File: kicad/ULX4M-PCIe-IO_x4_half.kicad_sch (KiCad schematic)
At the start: 51 parts, among them J10 FCR684205R, J11 OLED, J12 641737-1, J13 39-30-0060, J14 LM7805_EN, J15 POE, J3 SFP+, J4 SFP+, J5 HAT, J6 EXT_USB, J7 Micro_SD_Card_CD, J8 Board_To_Board, J9 FCR684205T, P1 HDMI-D, SW1 SW_DIP_x08, SW2 SW_DIP_x08, U10 TPD4E02B04DQA, U11 TPD4E02B04DQA, U12 TPD4E02B04DQA, U13 AT24CS32-SSHM, U14 LM78M05_TO252, U9 TPD4E02B04DQA

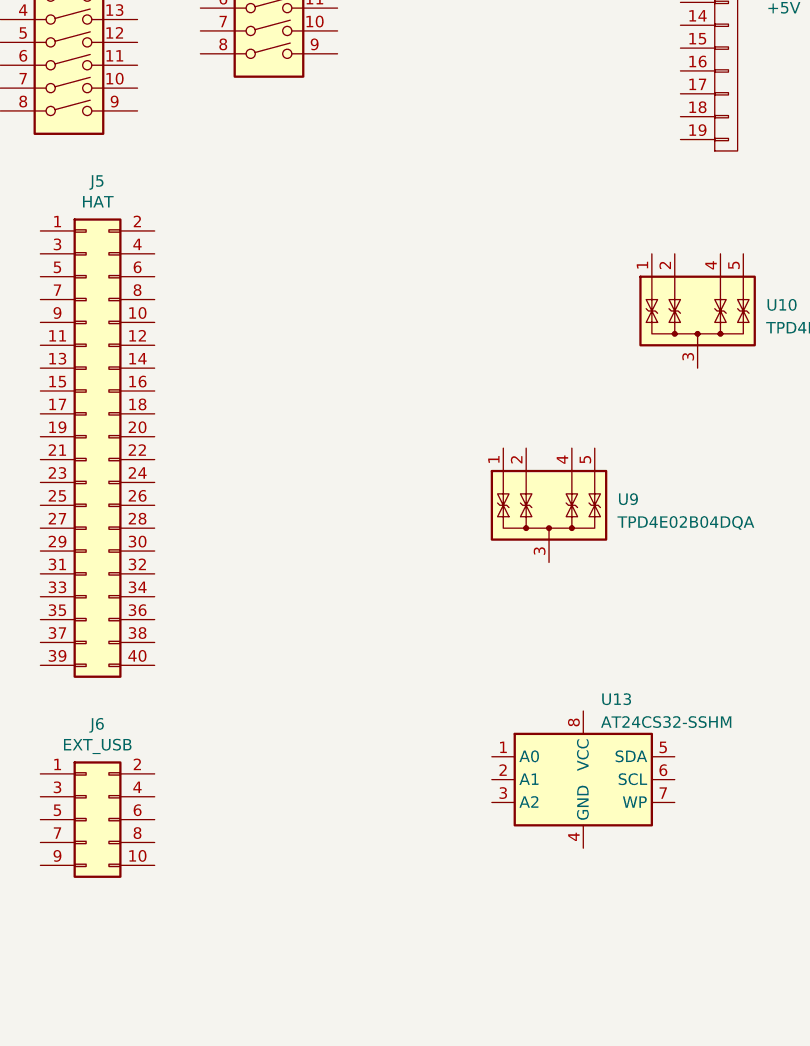
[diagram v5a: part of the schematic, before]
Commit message: Adding barrel connector, adding JTAG, adding new pic
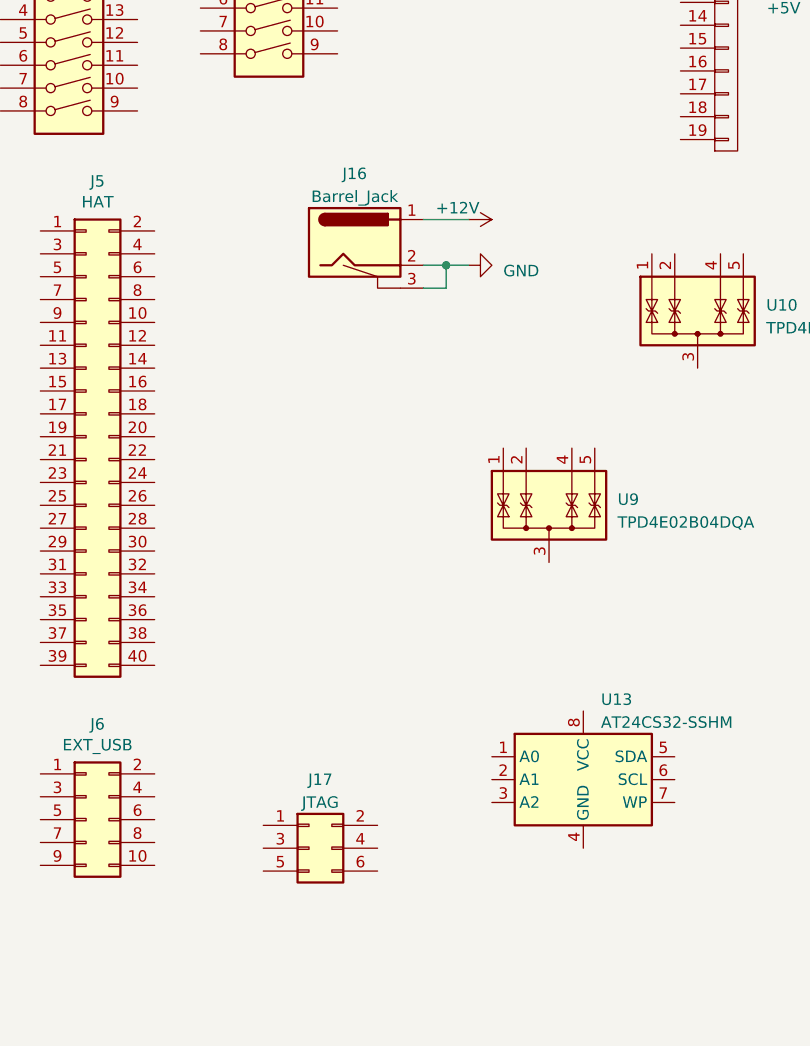
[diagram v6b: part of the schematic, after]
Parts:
- added J16: Barrel_Jack, CM4IO:BarrelJack_Horizontal, symbol CM4IO:Barrel_Jack
- added J17: JTAG, Connector_PinHeader_2.54mm:PinHeader_2x03_P2.54mm_Vertical, symbol Connector_Generic:Conn_02x03_Odd_Even
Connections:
- net +12V: now also J16.1
- net GND: now also J16.2, J16.3
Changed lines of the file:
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@@
   (junction (at 139.7 185.42) (diameter 0) (color 0 0 0 0)
   )
+  (junction (at 200.66 87.63) (diameter 0) (color 0 0 0 0)
+  )
   (junction (at 355.6 54.61) (diameter 0) (color 0 0 0 0)
   )
@@
     (stroke (width 0) (type default))
   )
+  (wire (pts (xy 198.12 87.63) (xy 200.66 87.63))
+    (stroke (width 0) (type default))
+  )
   (wire (pts (xy 355.6 54.61) (xy 365.76 54.61))
     (stroke (width 0) (type default))
   )
+  (wire (pts (xy 200.66 87.63) (xy 203.2 87.63))
+    (stroke (width 0) (type default))
+  )
   (wire (pts (xy 31.75 43.18) (xy 34.29 43.18))
     (stroke (width 0) (type default))
@@
     (stroke (width 0) (type default))
   )
+  (wire (pts (xy 200.66 90.17) (xy 200.66 87.63))
+    (stroke (width 0) (type default))
+  )
   (wire (pts (xy 167.64 187.96) (xy 165.1 187.96))
     (stroke (width 0) (type default))
@@
     (stroke (width 0) (type default))
   )
+  (wire (pts (xy 198.12 82.55) (xy 203.2 82.55))
+    (stroke (width 0) (type default))
+  )
   (wire (pts (xy 57.15 64.77) (xy 59.69 64.77))
+    (stroke (width 0) (type default))
+  )
+  (wire (pts (xy 198.12 90.17) (xy 200.66 90.17))
     (stroke (width 0) (type default))
   )
@@
     )
   )
+  (symbol (lib_id "Connector_Generic:Conn_02x03_Odd_Even") (at 185.42 152.4 0) (unit 1)
+    (in_bom yes) (on_board yes) (dnp no) (fields_autoplaced)
+    (property "Reference" "J17" (at 186.69 144.78 0)
+      (effects (font (size 1.27 1.27)))
+    )
+    (property "Value" "JTAG" (at 186.69 147.32 0)
+      (effects (font (size 1.27 1.27)))
+    )
+    (property "Footprint" "Connector_PinHeader_2.54mm:PinHeader_2x03_P2.54mm_Vertical" (at 185.42 152.4 0)
+      (effects (font (size 1.27 1.27)) hide)
+    )
+    (property "Datasheet" "~" (at 185.42 152.4 0)
+      (effects (font (size 1.27 1.27)) hide)
+    )
+    (pin "1")
+    (pin "2")
+    (pin "3")
+    (pin "4")
+    (pin "5")
+    (pin "6")
+    (instances
+      (project "ULX4M-PCIe-IO_x4_half"
+        (path "/e227bafe-08dc-4b2a-9df8-340d24e6faf1"
+          (reference "J17") (unit 1) (value "JTAG") (footprint "Connector_PinHeader_2.54mm:PinHeader_2x03_P2.54mm_Vertical")
+        )
+      )
+    )
+  )
   (symbol (lib_id "Mechanical:MountingHole") (at 80.01 193.04 0) (unit 1)
     (in_bom yes) (on_board yes) (dnp no) (fields_autoplaced)
@@
     )
   )
+  (symbol (lib_id "power:+12V") (at 203.2 82.55 270) (unit 1)
+    (in_bom yes) (on_board yes) (dnp no)
+    (property "Reference" "#PWR0107" (at 199.39 82.55 0)
+      (effects (font (size 1.27 1.27)) hide)
+    )
+    (property "Value" "+12V" (at 201.93 81.28 90)
+      (effects (font (size 1.27 1.27)))
+    )
+    (property "Footprint" "" (at 203.2 82.55 0)
+      (effects (font (size 1.27 1.27)) hide)
+    )
+    (property "Datasheet" "" (at 203.2 82.55 0)
+      (effects (font (size 1.27 1.27)) hide)
+    )
+    (pin "1")
+    (instances
+      (project "ULX4M-PCIe-IO_x4_half"
+        (path "/e227bafe-08dc-4b2a-9df8-340d24e6faf1/00000000-0000-0000-0000-00005d508b15"
+          (reference "#PWR0107") (unit 1) (value "+12V") (footprint "")
+        )
+        (path "/e227bafe-08dc-4b2a-9df8-340d24e6faf1"
+          (reference "#PWR0137") (unit 1) (value "+12V") (footprint "")
+        )
+      )
+    )
+  )
   (symbol (lib_id "Mechanical:MountingHole") (at 111.76 187.96 0) (unit 1)
     (in_bom yes) (on_board yes) (dnp no) (fields_autoplaced)
@@
         (path "/e227bafe-08dc-4b2a-9df8-340d24e6faf1"
           (reference "C11") (unit 1) (value "10nF") (footprint "Capacitor_SMD:C_0603_1608Metric")
+        )
+      )
+    )
+  )
+  (symbol (lib_id "power:GND") (at 203.2 87.63 90) (unit 1)
+    (in_bom yes) (on_board yes) (dnp no) (fields_autoplaced)
+    (property "Reference" "#PWR0138" (at 209.55 87.63 0)
+      (effects (font (size 1.27 1.27)) hide)
+    )
+    (property "Value" "GND" (at 207.01 88.265 90)
+      (effects (font (size 1.27 1.27)) (justify right))
+    )
+    (property "Footprint" "" (at 203.2 87.63 0)
+      (effects (font (size 1.27 1.27)) hide)
+    )
+    (property "Datasheet" "" (at 203.2 87.63 0)
+      (effects (font (size 1.27 1.27)) hide)
+    )
+    (pin "1")
+    (instances
+      (project "ULX4M-PCIe-IO_x4_half"
+        (path "/e227bafe-08dc-4b2a-9df8-340d24e6faf1"
+          (reference "#PWR0138") (unit 1) (value "GND") (footprint "")
         )
       )
@@
         )
       )
+    )
+  )
+  (symbol (lib_id "CM4IO:Barrel_Jack") (at 190.5 85.09 0) (unit 1)
+    (in_bom yes) (on_board yes) (dnp no) (fields_autoplaced)
+    (property "Reference" "J16" (at 190.5 77.47 0)
+      (effects (font (size 1.27 1.27)))
+    )
+    (property "Value" "Barrel_Jack" (at 190.5 80.01 0)
+      (effects (font (size 1.27 1.27)))
+    )
+    (property "Footprint" "CM4IO:BarrelJack_Horizontal" (at 191.77 86.106 0)
+      (effects (font (size 1.27 1.27)) hide)
+    )
+    (property "Datasheet" "" (at 191.77 86.106 0)
+      (effects (font (size 1.27 1.27)) hide)
+    )
+    (pin "1")
+    (pin "2")
+    (pin "3")
+    (instances
+      (project "ULX4M-PCIe-IO_x4_half"
+        (path "/e227bafe-08dc-4b2a-9df8-340d24e6faf1"
+          (reference "J16") (unit 1) (value "Barrel_Jack") (footprint "CM4IO:BarrelJack_Horizontal")
+        )
+      )

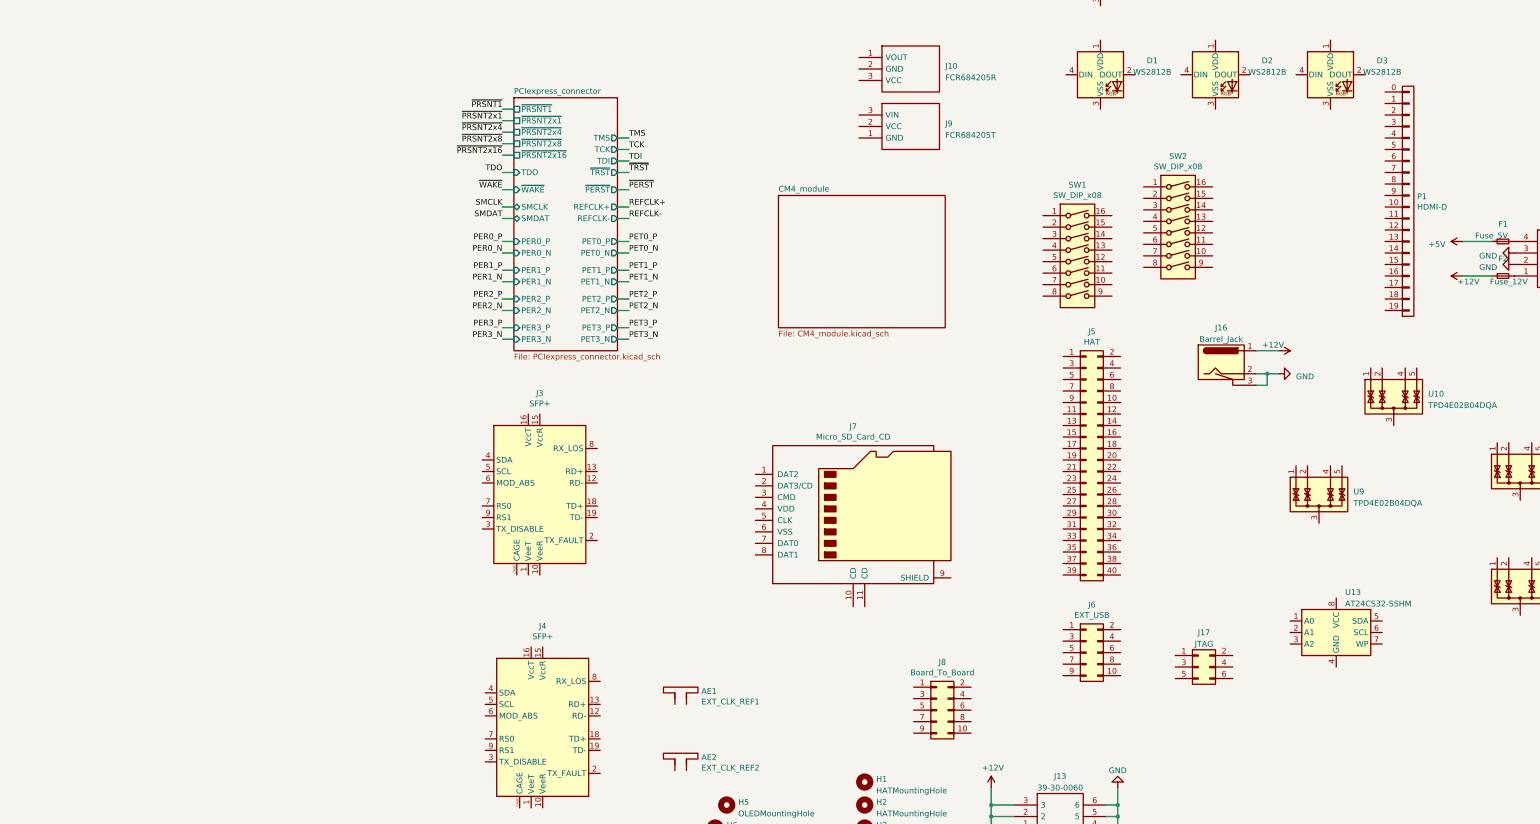
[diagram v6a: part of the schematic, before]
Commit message: Connecting GPIO, GPDI, B2B, SD
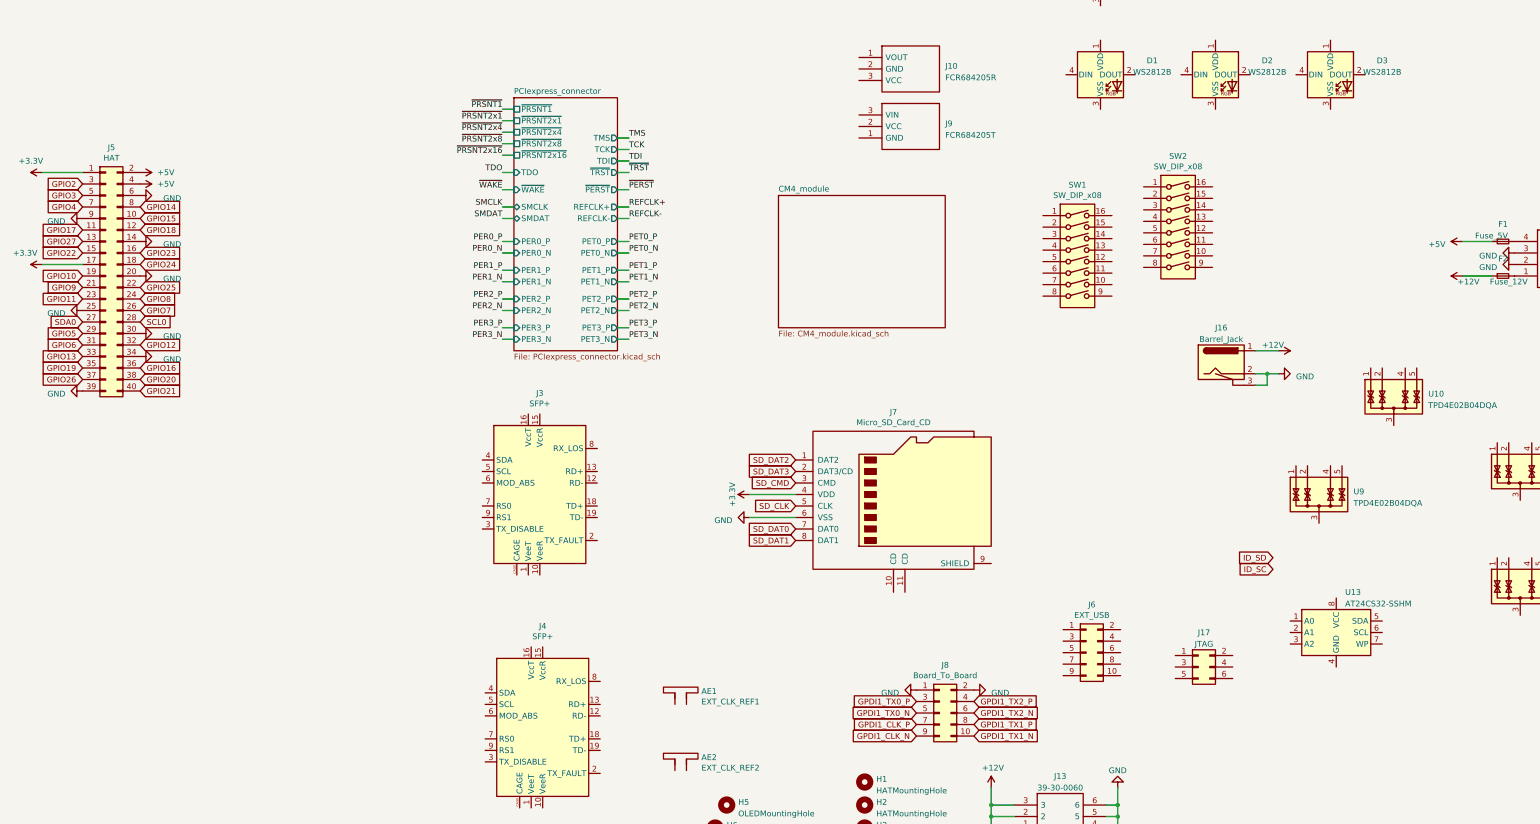
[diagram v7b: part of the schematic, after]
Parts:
- removed P1: HDMI-D, conn-fci:CONN-10029449-111RLF, symbol hdmi-d:HDMI-D
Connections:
- net +3.3V: now also J5.1 (Pin_1), J5.17 (Pin_17), J7.4 (VDD)
- net +5V: now also J5.2 (Pin_2), J5.4 (Pin_4)
- net GND: now also J5.14 (Pin_14), J5.20 (Pin_20), J5.25 (Pin_25), J5.30 (Pin_30), J5.34 (Pin_34), J5.39 (Pin_39), J5.6 (Pin_6), J5.9 (Pin_9), J7.6 (VSS), J8.1 (Pin_1), J8.2 (Pin_2)
- net GPDI1_TX1_N: now reaches J8.10 (Pin_10)
- net GPDI1_TX0_P: now reaches J8.3 (Pin_3)
- net GPDI1_TX2_P: now reaches J8.4 (Pin_4)
- net GPDI1_TX0_N: now reaches J8.5 (Pin_5)
- net GPDI1_TX2_N: now reaches J8.6 (Pin_6)
- net GPDI1_CLK_P: now reaches J8.7 (Pin_7)
- net GPDI1_TX1_P: now reaches J8.8 (Pin_8)
- net GPDI1_CLK_N: now reaches J8.9 (Pin_9)
- net GPIO15: now reaches J5.10 (Pin_10)
- net GPIO17: now reaches J5.11 (Pin_11)
- net GPIO18: now reaches J5.12 (Pin_12)
- net GPIO27: now reaches J5.13 (Pin_13)
- net GPIO22: now reaches J5.15 (Pin_15)
- net GPIO23: now reaches J5.16 (Pin_16)
- net GPIO24: now reaches J5.18 (Pin_18)
- net GPIO10: now reaches J5.19 (Pin_19)
- net GPIO9: now reaches J5.21 (Pin_21)
- net GPIO25: now reaches J5.22 (Pin_22)
- net GPIO11: now reaches J5.23 (Pin_23)
- net GPIO8: now reaches J5.24 (Pin_24)
- net GPIO7: now reaches J5.26 (Pin_26)
- net SDA0: now reaches J5.27 (Pin_27)
- net SCL0: now reaches J5.28 (Pin_28)
- net GPIO5: now reaches J5.29 (Pin_29)
- net GPIO2: now reaches J5.3 (Pin_3)
- net GPIO6: now reaches J5.31 (Pin_31)
- net GPIO12: now reaches J5.32 (Pin_32)
- net GPIO13: now reaches J5.33 (Pin_33)
- net GPIO19: now reaches J5.35 (Pin_35)
- net GPIO16: now reaches J5.36 (Pin_36)
- net GPIO26: now reaches J5.37 (Pin_37)
- net GPIO20: now reaches J5.38 (Pin_38)
- net GPIO21: now reaches J5.40 (Pin_40)
- net GPIO3: now reaches J5.5 (Pin_5)
- net GPIO4: now reaches J5.7 (Pin_7)
- net GPIO14: now reaches J5.8 (Pin_8)
- net SD_DAT2: now reaches J7.1 (DAT2)
- net SD_DAT3: now reaches J7.2 (DAT3/CD)
- net SD_CMD: now reaches J7.3 (CMD)
- net SD_CLK: now reaches J7.5 (CLK)
- net SD_DAT0: now reaches J7.7 (DAT0)
- net SD_DAT1: now reaches J7.8 (DAT1)
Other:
- moved on the sheet: J5, J7, J8

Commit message: Adding more connections - adding SFP parts
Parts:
- added C12, C15: 100n, Capacitor_SMD:C_0603_1608Metric, symbol Device:C_Small
- added C13, C14: 22u, Capacitor_SMD:C_0603_1608Metric, symbol Device:C_Small
- added FB1, FB2: FB, symbol Device:FerriteBead_Small
- added R13, R14, R15, R16, R17, R18, R19, R20, R21, R22: 4K7, Resistor_SMD:R_0603_1608Metric, symbol Device:R_Small
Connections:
- net +3.3V: now also J17.2 (Pin_2), U13.8 (VCC), FB1.1, FB2.2, R13.1, R14.1, R15.1, R16.1, R19.1, R20.1, R21.1, R22.1
- net GND: now also J17.1 (Pin_1), J3.1 (VeeT), J3.10 (VeeR), J3.11 (VeeR), J3.14 (VeeR), J3.17 (VeeT), J3.20 (VeeT), J3.CAGE, J4.1 (VeeT), J4.10 (VeeR), J4.11 (VeeR), J4.14 (VeeR), J4.17 (VeeT), J4.20 (VeeT), J4.CAGE, U13.1 (A0), U13.2 (A1), U13.3 (A2), U13.4 (GND), U13.7 (WP), C12.2, C13.2, C14.2, C15.2, R17.2, R18.2
- net GPIO12: now also J17.3 (Pin_3)
- net GPIO16: now also J17.6 (Pin_6)
- net GPIO20: now also J17.4 (Pin_4)
- net GPIO21: now also J17.5 (Pin_5)
- net ID_SC: now also U13.6 (SCL), R15.2
- net ID_SD: now also U13.5 (SDA), R16.2
- net SCL0: now also J3.5 (SCL), J4.5 (SCL), R13.2
- net SDA0: now also J3.4 (SDA), J4.4 (SDA), R14.2
- net SFP0_RX_N: now reaches J3.12 (RD-)
- net SFP0_RX_P: now reaches J3.13 (RD+)
- net VCCR: now reaches J3.15 (VccR)
- net VCCR: now also J4.15 (VccR), C14.1, C15.1, FB2.1
- net VCCT: now reaches J3.16 (VccT)
- net VCCT: now also J4.16 (VccT), C12.1, C13.1, FB1.2
- net SFP0_TX_P: now reaches J3.18 (TD+)
- net SFP0_TX_N: now reaches J3.19 (TD-)
- net at J3.2 (TX_FAULT): now also R20.2
- net at J3.3 (TX_DISABLE): now also R17.1
- net SFP0_MOD_ABS: now reaches J3.6 (MOD_ABS)
- net at J3.8 (RX_LOS): now also R19.2
- net SFP1_RX_N: now reaches J4.12 (RD-)
- net SFP1_RX_P: now reaches J4.13 (RD+)
- net SFP1_TX_P: now reaches J4.18 (TD+)
- net SFP1_TX_N: now reaches J4.19 (TD-)
- net at J4.2 (TX_FAULT): now also R22.2
- net at J4.3 (TX_DISABLE): now also R18.1
- net SFP1_MOD_ABS: now reaches J4.6 (MOD_ABS)
- net at J4.8 (RX_LOS): now also R21.2
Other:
- moved on the sheet: J17, J3, J4
